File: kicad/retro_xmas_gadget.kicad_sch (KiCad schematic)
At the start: 26 parts, among them J1 USB_C_Receptacle_USB2.0_16P, J2 SD_Card_Receptacle, J3 AudioJack3_SwitchTR, Q1 UMH3N, SW1 RESET, SW2 BOOT, SW3 SW_SPDT, U1 CP2102N-Axx-xQFN28, U2 ESP32-S3-WROOM-1

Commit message: complete most of design
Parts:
- added C10, C11, C14, C15: 100nf, Capacitor_SMD:C_0603_1608Metric_Pad1.08x0.95mm_HandSolder, symbol Device:C
- added C12, C13, C9: 10uf, Capacitor_SMD:C_0603_1608Metric_Pad1.08x0.95mm_HandSolder, symbol Device:C
- added H1, H2, H3, H4: MountingHole, MountingHole:MountingHole_2.7mm_M2.5, symbol Mechanical:MountingHole
- added J4: Conn_01x18, Connector_FFC-FPC:TE_1-1734839-8_1x18-1MP_P0.5mm_Horizontal, symbol Connector_Generic:Conn_01x18
- added J5: Conn_01x02, Connector_JST:JST_SH_SM02B-SRSS-TB_1x02-1MP_P1.00mm_Horizontal, symbol Connector_Generic:Conn_01x02
- added J6: Conn_01x03, Connector_JST:JST_GH_SM03B-GHS-TB_1x03-1MP_P1.25mm_Horizontal, symbol Connector_Generic:Conn_01x03
- added J7: Conn_01x03, Connector_PinHeader_2.54mm:PinHeader_1x03_P2.54mm_Vertical, symbol Connector_Generic:Conn_01x03
- added Q2: SS8050, Package_TO_SOT_SMD:SOT-23, symbol Transistor_BJT:SS8050
- added R10: 470, Resistor_SMD:R_0603_1608Metric_Pad0.98x0.95mm_HandSolder, symbol Device:R
- added R11, R12: 100K, Resistor_SMD:R_0603_1608Metric_Pad0.98x0.95mm_HandSolder, symbol Device:R
- added R13, R9: 10k, Resistor_SMD:R_0603_1608Metric_Pad0.98x0.95mm_HandSolder, symbol Device:R
- added R14: 2K, Resistor_SMD:R_0603_1608Metric_Pad0.98x0.95mm_HandSolder, symbol Device:R
- added R15: 5.1k, Resistor_SMD:R_0603_1608Metric_Pad0.98x0.95mm_HandSolder, symbol Device:R
- added R16: 1k, Resistor_SMD:R_0603_1608Metric_Pad0.98x0.95mm_HandSolder, symbol Device:R
- added R17: 0, Capacitor_SMD:C_0402_1005Metric, symbol Device:R
- added R18: 0, Resistor_SMD:R_0603_1608Metric_Pad0.98x0.95mm_HandSolder, symbol Device:R
- added R19: 1K, Resistor_SMD:R_0603_1608Metric_Pad0.98x0.95mm_HandSolder, symbol Device:R
- added R20: 10K, symbol Device:R
- added R21: 10R, Resistor_SMD:R_0603_1608Metric_Pad0.98x0.95mm_HandSolder, symbol Device:R
- added U3: ~, Package_SO:SOP-8-1EP_4.57x4.57mm_P1.27mm_EP4.57x4.45mm_ThermalVias, symbol NS4168:NS4168
- added U4: XC6210B332MR, Package_TO_SOT_SMD:SOT-23-5, symbol Regulator_Linear:XC6210B332MR
- added U5: TP4056, Package_SO:SOP-8-1EP_4.57x4.57mm_P1.27mm_EP4.57x4.45mm_ThermalVias, symbol TP4056:TP4056
- C5, C6: footprint (none) -> Capacitor_SMD:C_0603_1608Metric_Pad1.08x0.95mm_HandSolder
- R5, R6, R7, R8: footprint (none) -> Resistor_SMD:R_0603_1608Metric_Pad0.98x0.95mm_HandSolder
- SW1, SW2: footprint (none) -> Button_Switch_SMD:SW_Push_SPST_NO_Alps_SKRK
- SW3: value SW_SPDT -> KH-SS12F23-G6
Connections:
- net GND: now also C10.2, C11.2, C12.1, C13.2, C14.2, C15.2, C9.2, J4.1 (Pin_1), J4.8 (Pin_8), J6.3 (Pin_3), J7.1 (Pin_1), Q2.2 (E), R12.2, R14.2, U3.7 (GND), U4.2 (GND), U5.1 (TEMP), U5.3 (GND)
- net IO4: now also C11.1, R11.2, R12.1
- net RXD: now also J7.2 (Pin_2)
- net TXD: now also J7.3 (Pin_3)
- net VBUS: now also C14.1, R15.2, R16.1, U5.4 (VCC), U5.8 (CE)
- net VCC: now also C10.1, C13.1, C15.1, C9.1, J4.9 (Pin_9), R20.2, R21.1, R9.1, U3.6 (VDD), U4.5 (VOUT)
- net VBAT: now reaches SW3.2 (B)
- net VBAT: now also U5.5 (BAT)
- net VBAT_ON: now reaches SW3.3 (C)
- net VBAT_ON: now also C12.2, J6.1 (Pin_1), R11.1, R13.1, U4.1 (VIN)
- net at C3.1, C4.1, U1.6 (VDD): now also R17.2; no longer U1.7 (VREGIN)
- net HJ+: now reaches J3.R
- net HJ+: now also J3.T, R10.1
- net SPK+: now reaches J3.RN
- net SPK+: now also J5.1 (Pin_1)
- net AUDIO-: now reaches J3.S
- net AUDIO-: now also J5.2 (Pin_2), U3.5 (VON)
- net AUDIO+: now reaches J3.TN
- net AUDIO+: now also R10.2, U3.8 (VOP)
- net IO10 renamed SD_CD
- net IO11 renamed SD_CMD
- net IO12 renamed TFT_SDI
- net TFT_SDI: now also J4.6 (Pin_6)
- net IO13 renamed SD_CLK
- net IO14 renamed TFT_CS
- net TFT_CS: now also J4.5 (Pin_5)
- net IO3 renamed TFT_RST
- net TFT_RST: now also J4.2 (Pin_2)
- net IO39 renamed TFT_LED
- net TFT_LED: now also R19.1
- net IO40 renamed AMP_DATA
- net AMP_DATA: now also U3.4 (SDATA)
- net IO41 renamed AMP_BCLK
- net AMP_BCLK: now also U3.3 (BCLK)
- net IO42 renamed AMP_LRCLK
- net AMP_LRCLK: now also U3.2 (LRCLK)
- net IO47 renamed TFT_DC
- net TFT_DC: now also J4.4 (Pin_4)
- net IO48 renamed TFT_SCL
- net TFT_SCL: now also J4.3 (Pin_3)
- net IO9 renamed SD_DAT
- new net: R13.2, U4.3 (CE)
- new net: R9.2, U3.1 (CTRL)
- new net: R15.1, U5.6 (~{STDBY})
- new net: Q2.1 (B), R19.2, R20.1
- new net: Q2.3 (C), R18.1
- new net: R14.1, U5.2 (PROG)
- new net: R17.1, U1.7 (VREGIN)
- new net: R16.2, U5.7 (~{CHRG})
- new net TFT_LEDA: J4.10 (Pin_10), R21.2
- new net TFT_LEDK: J4.11 (Pin_11), J4.12 (Pin_12), J4.13 (Pin_13), J4.14 (Pin_14), R18.2
- new net TFT_SDO: J4.7 (Pin_7)
- no-connect marks 10 -> 19
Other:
- note added: "Battery"
- note added: "Battery Monitor"
- note added: "Battery thermal sensor"
- note added: "Check headphone jack"
- note added: "Class D Amp"
- note added: "Display"
- note added: "Headphone Jack"
- note added: "Speaker"
- note added: "Voltage Regulator"
- note added: "Volume potentiometer"
- note added: "replace voltage regulator"
- note added: "status led"
- moved on the sheet: C5, C6, C7, C8, J2, J3, Q1A, Q1B, R5, R6, R7, R8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

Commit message: initial board layout
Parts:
- added SW10: SELECT, Button_Switch_SMD:SW_SPST_SKQG_WithStem, symbol Switch:SW_Push
- added SW11: START, Button_Switch_SMD:SW_SPST_SKQG_WithStem, symbol Switch:SW_Push
- added SW12: A, Button_Switch_SMD:SW_SPST_SKQG_WithStem, symbol Switch:SW_Push
- added SW13: B, Button_Switch_SMD:SW_SPST_SKQG_WithStem, symbol Switch:SW_Push
- added SW4: UP, Button_Switch_SMD:SW_SPST_SKQG_WithStem, symbol Switch:SW_Push
- added SW5: DOWN, Button_Switch_SMD:SW_SPST_SKQG_WithStem, symbol Switch:SW_Push
- added SW6: LEFT, Button_Switch_SMD:SW_SPST_SKQG_WithStem, symbol Switch:SW_Push
- added SW7: RIGHT, Button_Switch_SMD:SW_SPST_SKQG_WithStem, symbol Switch:SW_Push
- added SW8: MENU, Button_Switch_SMD:SW_SPST_SKQG_WithStem, symbol Switch:SW_Push
- added SW9: OPTION, Button_Switch_SMD:SW_SPST_SKQG_WithStem, symbol Switch:SW_Push
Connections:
- net GND: now also SW10.2, SW11.2, SW12.2, SW13.2, SW4.2, SW5.2, SW6.2, SW7.2, SW8.2, SW9.2
- net IO0 renamed BOOT
- net IO15 renamed KEY_A
- net KEY_A: now also SW12.1
- net IO16 renamed KEY_SELECT
- net KEY_SELECT: now also SW10.1
- net IO17 renamed KEY_START
- net KEY_START: now also SW11.1
- net IO18 renamed KEY_MENU
- net KEY_MENU: now also SW8.1
- net IO38 renamed LED_STATUS
- net IO4 renamed VBAT_SENSE
- net IO5 renamed KEY_B
- net KEY_B: now also SW13.1
- net IO6 renamed KEY_RIGHT
- net KEY_RIGHT: now also SW7.1
- net IO7 renamed KEY_UP
- net KEY_UP: now also SW4.1
- net IO8 renamed KEY_OPTION
- net KEY_OPTION: now also SW9.1
- new net KEY_DOWN: SW5.1
- new net KEY_LEFT: SW6.1
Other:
- note added: "Buttons"
- note added: "Charge Leds"
- note added: "Controlled impedance for USB D- and D+?"
- note added: "Expander GPIO"
- note added: "Extra GPIO"
- note added: "Keys"
- note added: "Status LED"
- note removed: "Volume potentiometer"
- note removed: "replace voltage regulator"
- moved on the sheet: C15, C5, C6, C7, C8, J2, J3, J4, J5, J7, Q1A, Q1B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

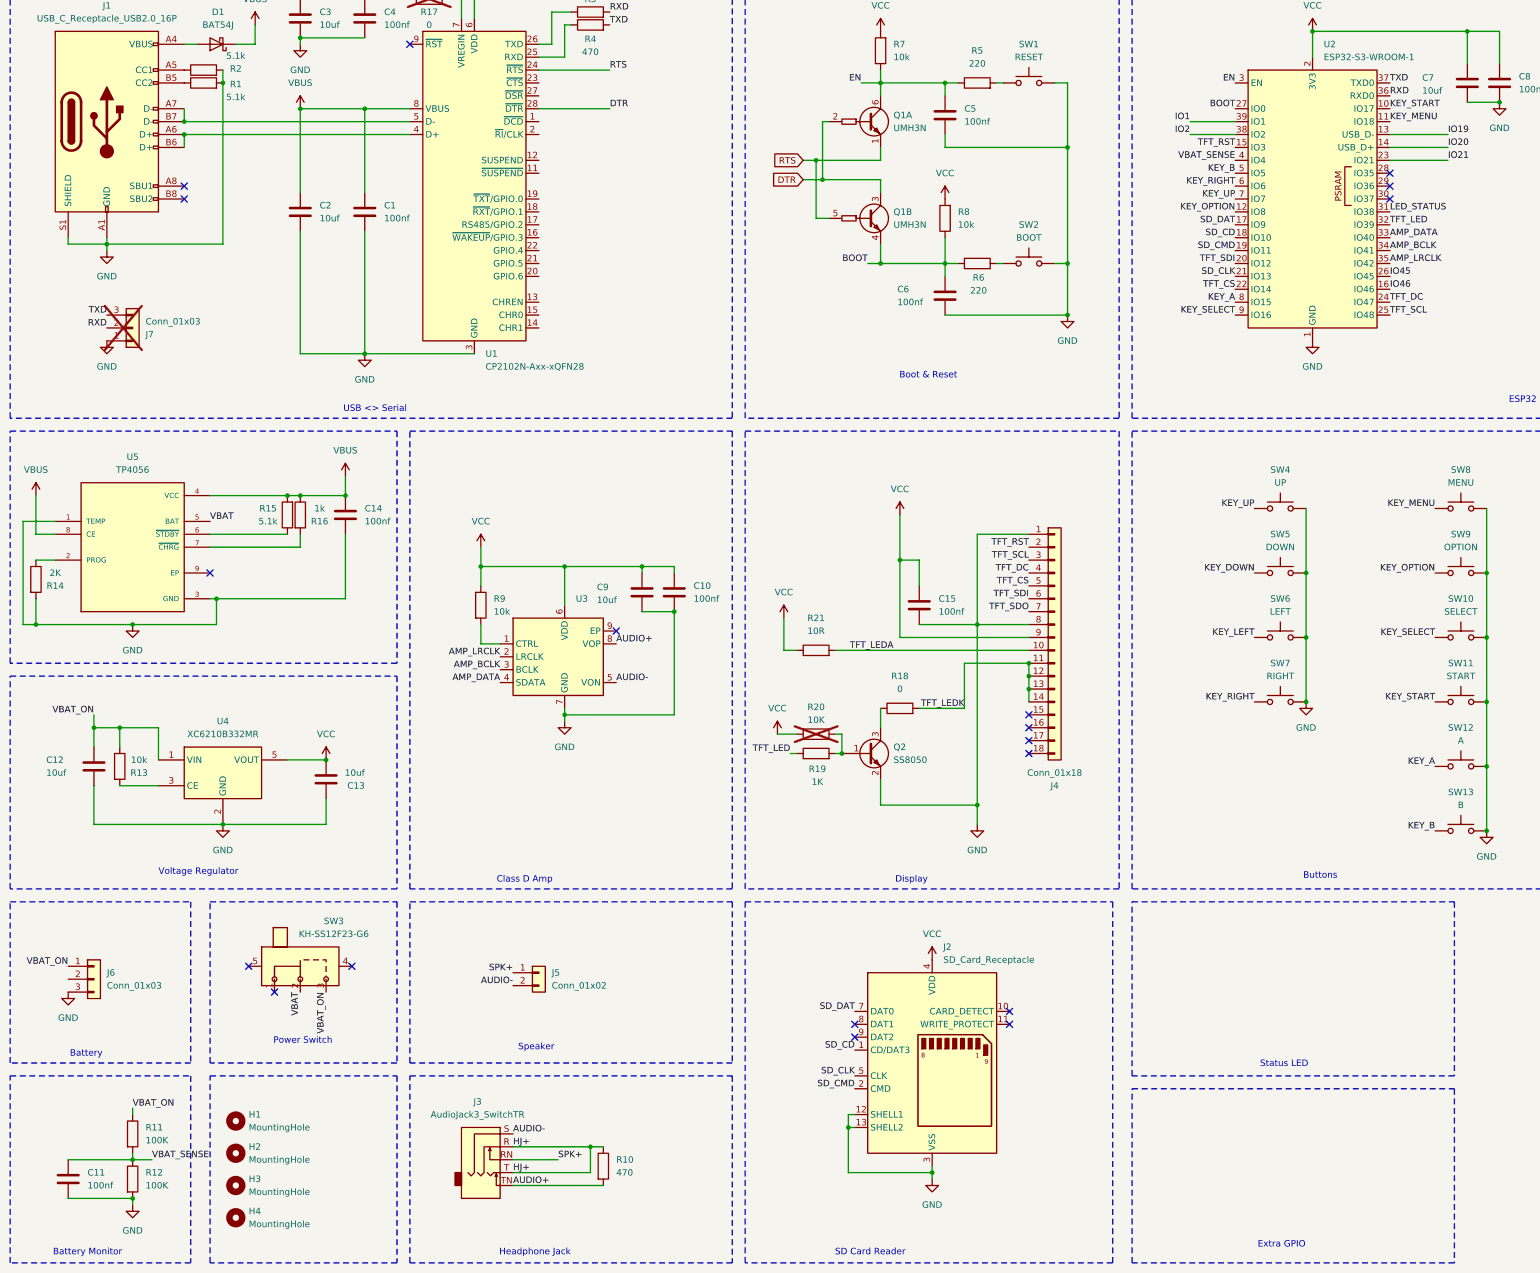
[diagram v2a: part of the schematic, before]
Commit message: button positioning and routing
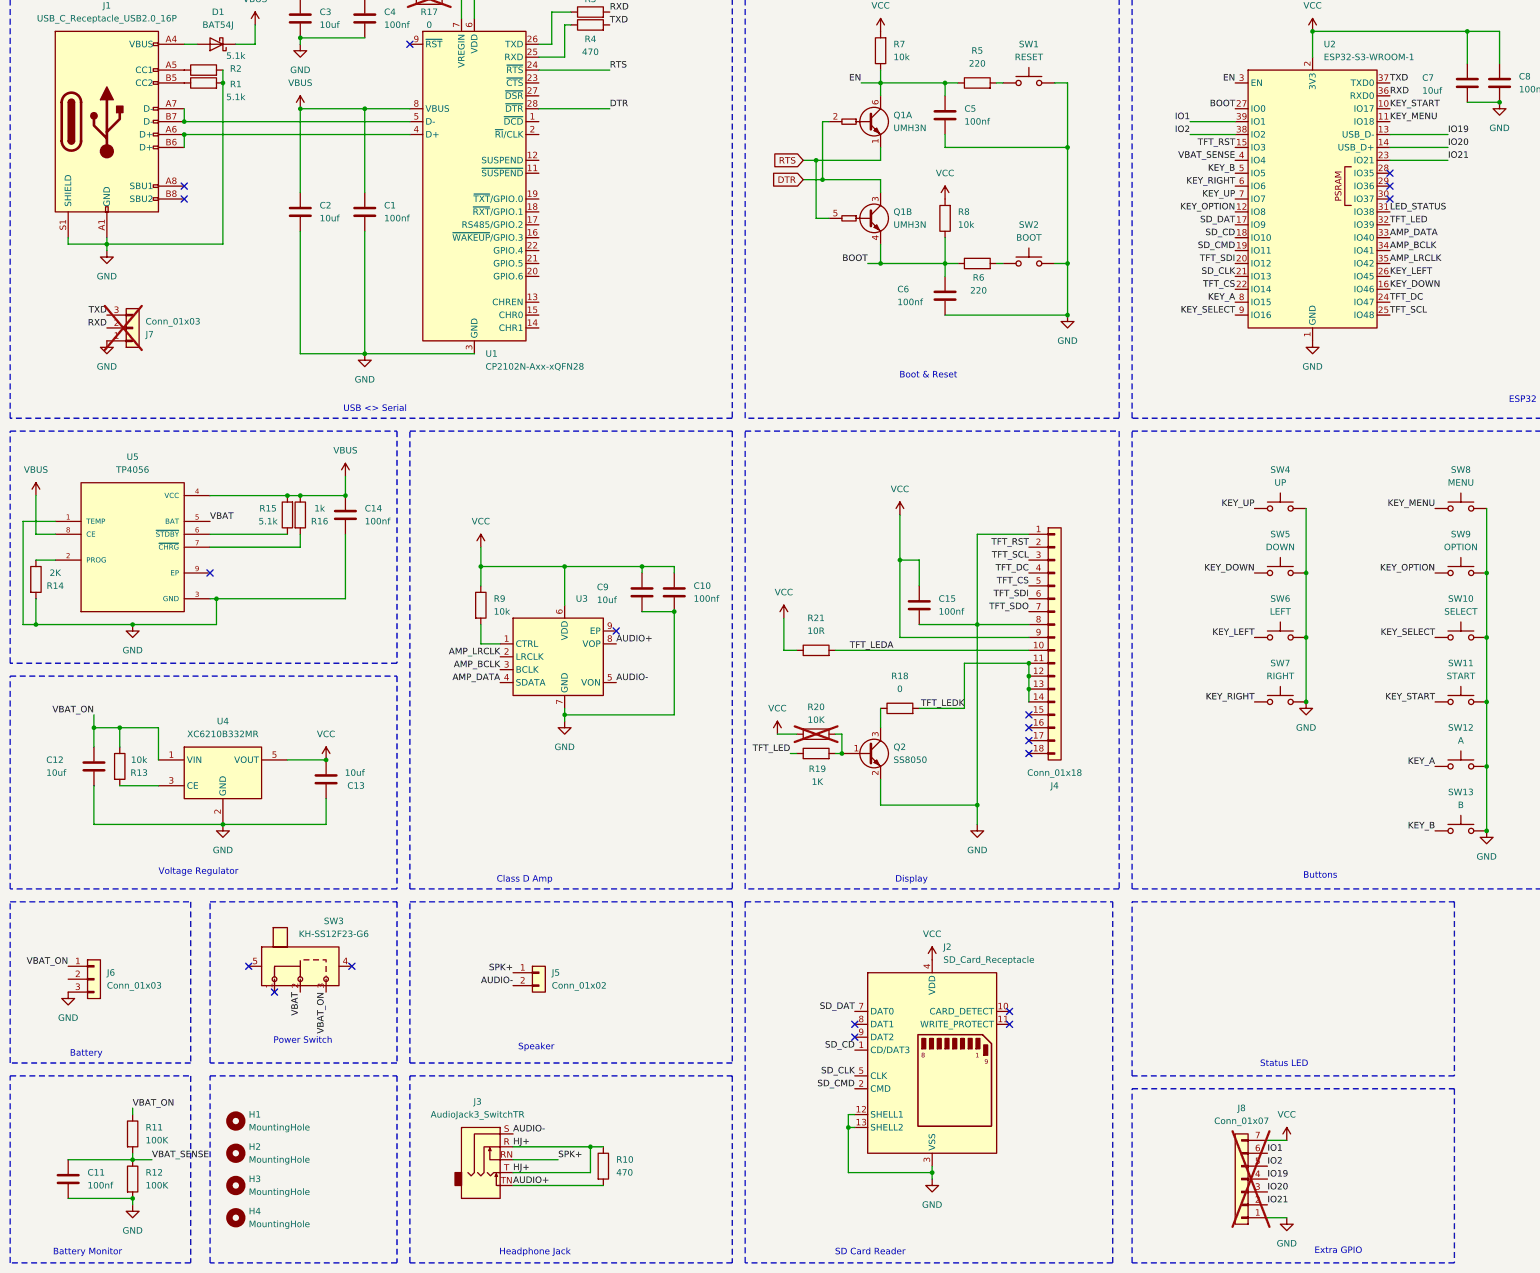
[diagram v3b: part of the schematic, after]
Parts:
- added J8: Conn_01x07, Connector_JST:JST_GH_SM07B-GHS-TB_1x07-1MP_P1.25mm_Horizontal, symbol Connector_Generic:Conn_01x07
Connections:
- net IO45 is gone; now on net KEY_LEFT: U2.26 (IO45)
- net IO46 is gone; now on net KEY_DOWN: U2.16 (IO46)
- net GND: now also J8.1 (Pin_1)
- net IO1: now also J8.6 (Pin_6)
- net IO19: now also J8.4 (Pin_4)
- net IO2: now also J8.5 (Pin_5)
- net IO20: now also J8.3 (Pin_3)
- net IO21: now also J8.2 (Pin_2)
- net VCC: now also J8.7 (Pin_7)

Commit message: stitching
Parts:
- added D2: RED, LED_SMD:LED_0805_2012Metric_Pad1.15x1.40mm_HandSolder, symbol Device:LED
- added D3: GREEN, LED_SMD:LED_0805_2012Metric_Pad1.15x1.40mm_HandSolder, symbol Device:LED
- added D4: ORANGE, LED_SMD:LED_0805_2012Metric_Pad1.15x1.40mm_HandSolder, symbol Device:LED
- added R22: 1K, Resistor_SMD:R_0603_1608Metric_Pad0.98x0.95mm_HandSolder, symbol Device:R
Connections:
- net GND: now also D2.1 (K)
- net LED_STATUS: now also R22.1
- net VBUS: now also D3.2 (A), D4.2 (A); no longer R15.2, R16.1
- new net: D4.1 (K), R16.1
- new net: D2.2 (A), R22.2
- new net: D3.1 (K), R15.2
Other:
- moved on the sheet: R15, R16

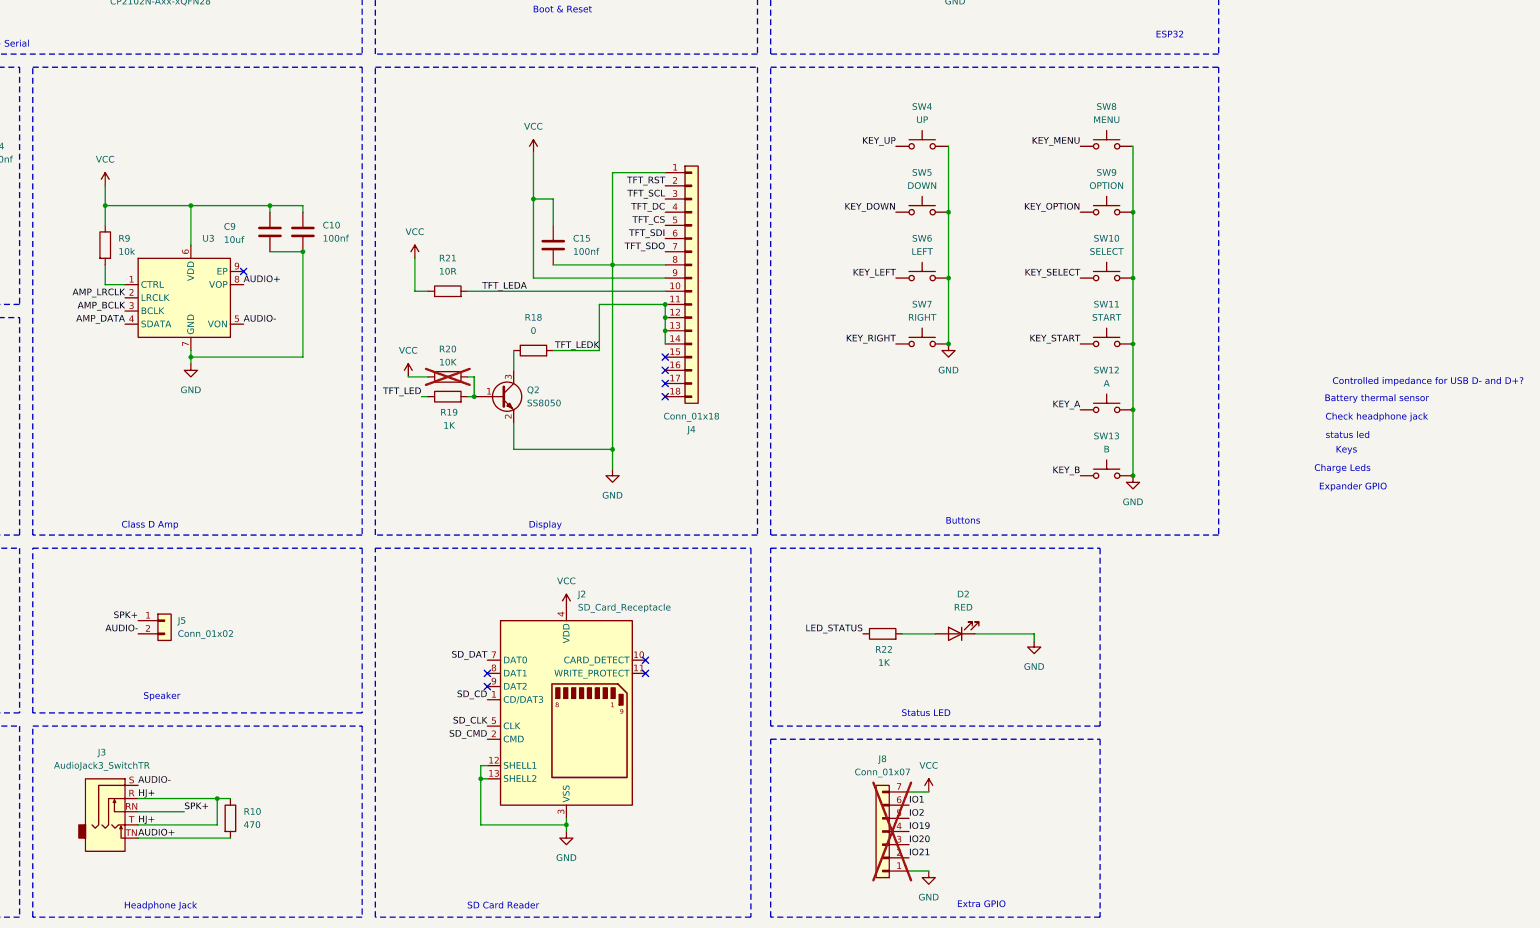
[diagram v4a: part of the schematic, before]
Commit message: change to 4 layer pcb
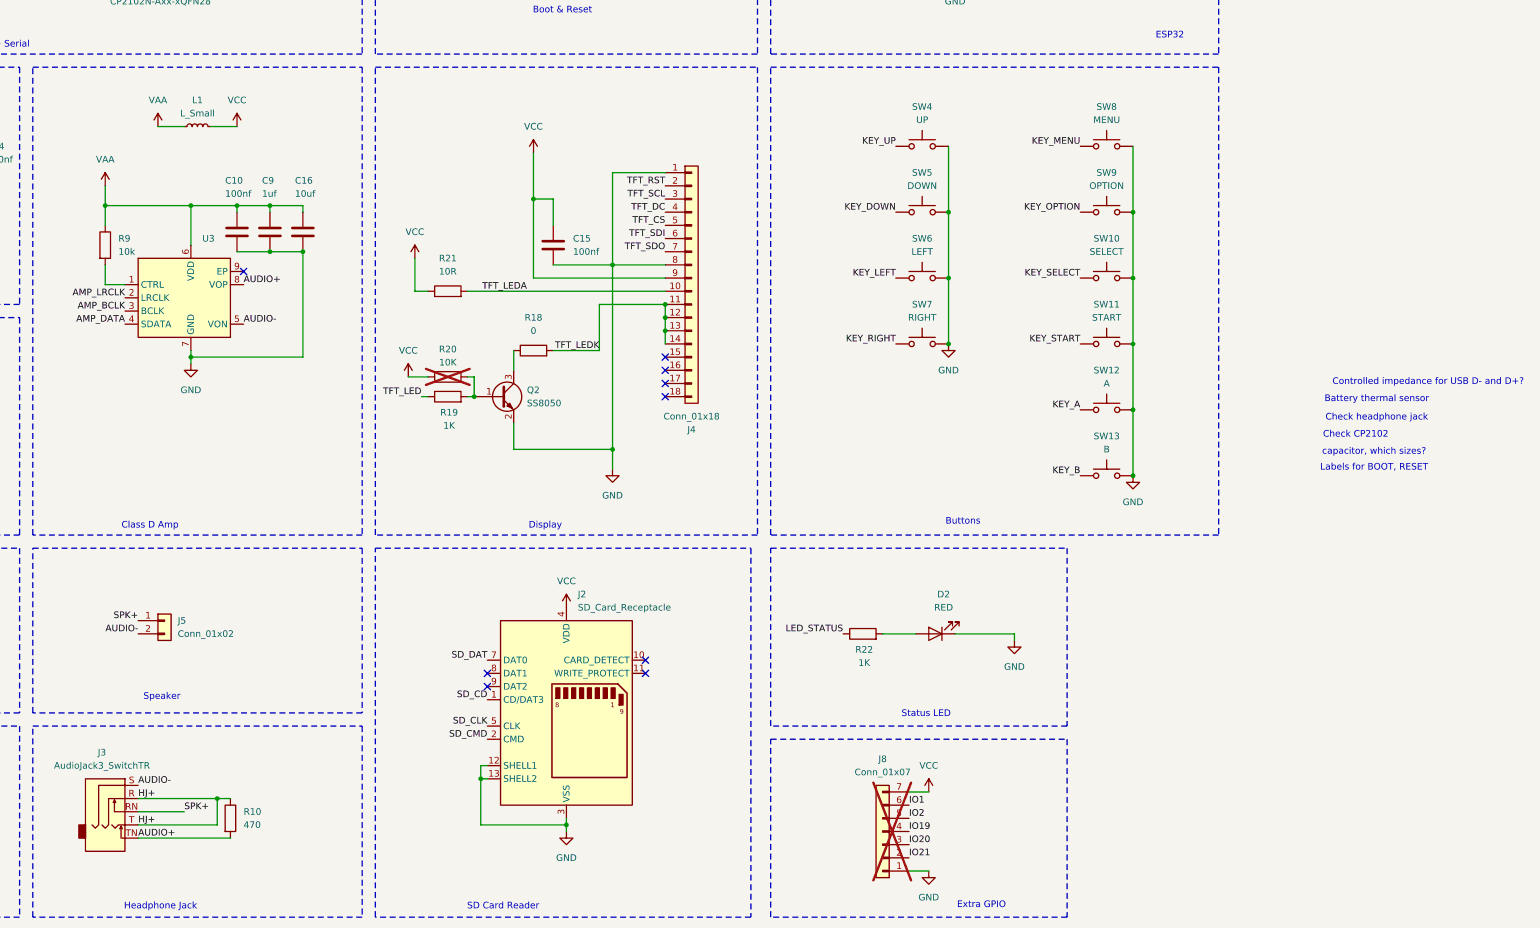
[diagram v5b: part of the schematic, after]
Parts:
- added C16: 10uf, Capacitor_SMD:C_0805_2012Metric_Pad1.18x1.45mm_HandSolder, symbol Device:C
- added L1: L_Small, Inductor_SMD:L_0603_1608Metric_Pad1.05x0.95mm_HandSolder, symbol Device:L_Small
- C9: value 10uf -> 1uf
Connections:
- net GND: now also C16.2
- net VCC: now also L1.2; no longer C10.1, C9.1, R9.1, U3.6 (VDD)
- new net VAA: C10.1, C16.1, C9.1, L1.1, R9.1, U3.6 (VDD)
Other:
- note added: "Check CP2102"
- note added: "Labels for BOOT, RESET"
- note added: "capacitor, which sizes?"
- note removed: "Charge Leds"
- note removed: "Expander GPIO"
- note removed: "Keys"
- note removed: "status led"
- moved on the sheet: C10, D2, R22
